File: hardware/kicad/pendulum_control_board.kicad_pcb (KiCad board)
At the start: 2 copper layers, 106.5 x 112.9 mm, 269 parts, among them IC1 STM32F411CEU6, IC2 LM358D, J1 DX07S024JJ2, Q1 BSS138, Q2 BSS138, Q3 BSS138, Q4 BSS138, Q5 2N7002, Q6 2N7002, Q7 2N7002, U1 FT231XS, U2 V_REG_317SMD, U3 V_REG_317SMD, U5 LTC6102DD, X1 5566-8, X2 5566-8, Y2 32.768kHz

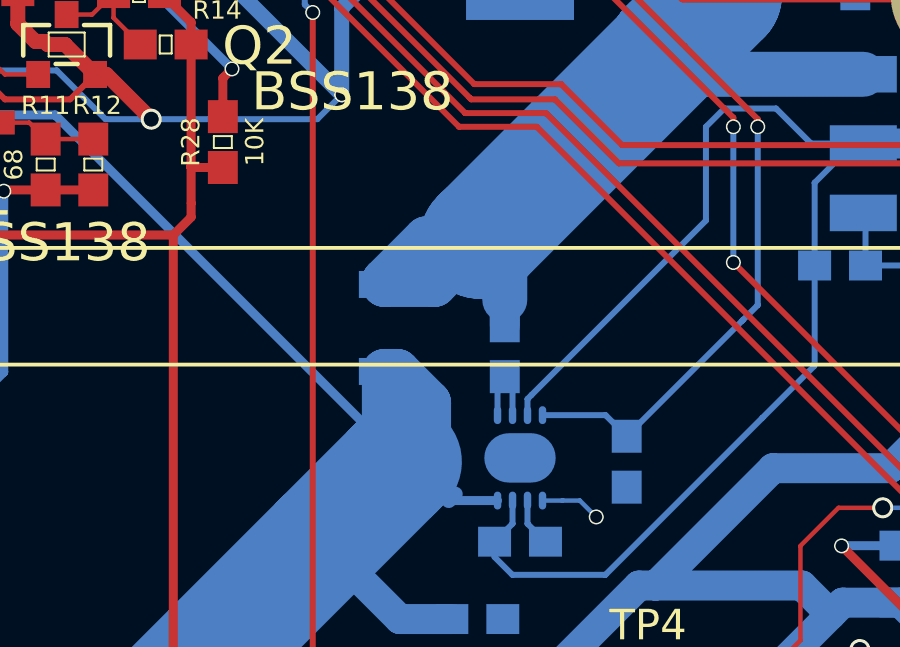
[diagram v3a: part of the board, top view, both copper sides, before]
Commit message: moved interfering resistor
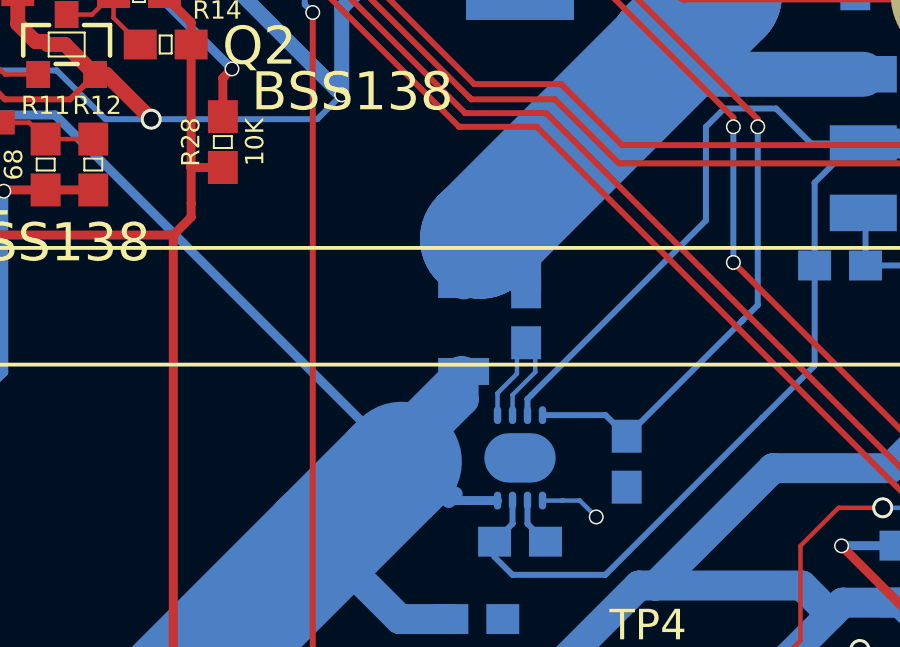
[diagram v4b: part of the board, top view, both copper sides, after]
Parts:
- moved R99 2.64 mm to (92.9, 125.0)
- moved R98 1.34 mm to (94.9, 124.7)
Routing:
- net /V_BATT: track 221.7 -> 210.1 mm
- net /N$85: track 2.77 -> 5.66 mm
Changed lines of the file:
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@@
     (links 735)
     (no_connects 0)
-    (area 47.536899 49.987999 154.177201 163.016401)
+    (area 44.840853 49.987999 154.177201 163.209581)
     (thickness 1.6)
     (drawings 6)
-    (tracks 2904)
+    (tracks 2903)
     (zones 0)
     (modules 269)
@@
   )
   (setup
-    (last_trace_width 0.3)
+    (last_trace_width 0.15)
     (user_trace_width 0.15)
     (user_trace_width 0.2)
@@
   )
   (module SPARKFUN-RESISTORS_0603 (layer B.Cu)
-    (at 94.234 125.7935 270)
+    (at 94.9452 124.6632 270)
     (descr "GENERIC 1608 (0603) PACKAGE")
     (tags "GENERIC 1608 (0603) PACKAGE")
@@
   )
   (module Resistors_SMD:R_1206 (layer B.Cu)
-    (at 90.2208 125.0188 90)
+    (at 92.8624 125.0188 90)
     (descr "Resistor SMD 1206, reflow soldering, Vishay (see dcrcw.pdf)")
     (tags "resistor 1206")
     (attr smd)
-    (fp_text reference R99 (at 0 2.3 90) (layer B.SilkS)
+    (fp_text reference R99 (at 0.254 -2.4892 90) (layer B.SilkS)
       (effects (font (size 1 1) (thickness 0.15)) (justify mirror))
     )
-    (fp_text value 1m (at 0 -2.3 90) (layer B.Fab)
+    (fp_text value 1m (at 0 -2.3 90) (layer B.Fab) hide
       (effects (font (size 1 1) (thickness 0.15)) (justify mirror))
     )
@@
   (segment (start 108.1024 148.6154) (end 106.77652 148.6154) (width 0.15) (layer B.Cu) (net 1))
   (segment (start 72.7075 101.68636) (end 72.263 101.68636) (width 0.15) (layer F.Cu) (net 1))
-  (segment (start 90.2208 123.5688) (end 90.2208 123.444) (width 1.5) (layer B.Cu) (net 2))
-  (segment (start 90.2208 123.444) (end 91.6178 122.047) (width 1.5) (layer B.Cu) (net 2))
-  (segment (start 91.6178 122.047) (end 93.4085 122.047) (width 1.5) (layer B.Cu) (net 2))
-  (segment (start 90.2208 123.5688) (end 91.8867 123.5688) (width 1.5) (layer B.Cu) (net 2))
-  (segment (start 91.8867 123.5688) (end 93.5355 121.92) (width 1.5) (layer B.Cu) (net 2))
+  (segment (start 94.9452 123.81484) (end 94.9452 120.6627) (width 1) (layer B.Cu) (net 2))
+  (segment (start 94.869 120.5865) (end 94.234 121.2215) (width 1) (layer B.Cu) (net 2))
+  (segment (start 94.9452 120.6627) (end 94.869 120.5865) (width 1) (layer B.Cu) (net 2))
+  (segment (start 92.8624 123.5688) (end 92.8624 122.5931) (width 1) (layer B.Cu) (net 2))
+  (segment (start 93.4085 122.047) (end 99.695 115.7605) (width 4) (layer B.Cu) (net 2))
+  (segment (start 93.5355 121.92) (end 93.4085 122.047) (width 4) (layer B.Cu) (net 2))
+  (segment (start 92.8624 122.5931) (end 93.5355 121.92) (width 1) (layer B.Cu) (net 2))
   (segment (start 95.08236 97.282) (end 96.5835 97.282) (width 0.2) (layer B.Cu) (net 2))
   (segment (start 96.5835 97.282) (end 98.1075 95.758) (width 0.2) (layer B.Cu) (net 2))
@@
   (segment (start 97.05086 107.4547) (end 101.1682 107.4547) (width 1.5) (layer B.Cu) (net 2))
   (segment (start 101.1682 107.4547) (end 101.473 107.7595) (width 1.5) (layer B.Cu) (net 2))
-  (segment (start 93.5355 121.92) (end 93.4085 122.047) (width 4) (layer B.Cu) (net 2))
-  (segment (start 93.4085 122.047) (end 99.695 115.7605) (width 4) (layer B.Cu) (net 2))
   (segment (start 101.473 113.919) (end 101.473 107.7595) (width 4) (layer B.Cu) (net 2))
   (segment (start 99.695 115.697) (end 101.473 113.919) (width 4) (layer B.Cu) (net 2))
   (segment (start 99.695 115.7605) (end 99.695 115.697) (width 4) (layer B.Cu) (net 2))
-  (segment (start 94.234 121.2215) (end 94.234 124.079) (width 1.5) (layer B.Cu) (net 2))
-  (segment (start 94.234 124.94514) (end 94.234 124.079) (width 1) (layer B.Cu) (net 2))
-  (segment (start 93.5355 121.92) (end 94.234 121.2215) (width 1.5) (layer B.Cu) (net 2))
-  (segment (start 94.234 121.2215) (end 92.583 122.8725) (width 1.5) (layer B.Cu) (net 2))
-  (segment (start 93.5355 121.92) (end 94.869 120.5865) (width 1) (layer B.Cu) (net 2))
-  (segment (start 94.234 121.2215) (end 94.869 120.5865) (width 1) (layer B.Cu) (net 2))
   (segment (start 104.56164 122.936) (end 104.56164 126.27356) (width 0.2) (layer B.Cu) (net 3))
   (segment (start 93.89364 132.65404) (end 94.488 133.2484) (width 0.2) (layer B.Cu) (net 3))
@@
   (segment (start 61.8236 103.9876) (end 60.94476 103.9876) (width 0.15) (layer F.Cu) (net 15))
   (segment (start 63.21298 105.37698) (end 61.8236 103.9876) (width 0.15) (layer F.Cu) (net 15))
-  (segment (start 90.2208 126.4688) (end 90.6548 126.4688) (width 1.5) (layer B.Cu) (net 16))
-  (segment (start 90.6548 126.4688) (end 91.694 127.508) (width 1.5) (layer B.Cu) (net 16))
+  (segment (start 92.8624 126.4688) (end 92.8624 127.4191) (width 1) (layer B.Cu) (net 16))
+  (segment (start 92.8624 127.4191) (end 91.694 128.5875) (width 1) (layer B.Cu) (net 16))
   (segment (start 91.694 128.5875) (end 90.805 129.4765) (width 1.5) (layer B.Cu) (net 16))
-  (segment (start 91.694 127.508) (end 91.694 128.5875) (width 1.5) (layer B.Cu) (net 16))
-  (segment (start 90.2208 126.4688) (end 90.2208 128.8923) (width 1.5) (layer B.Cu) (net 16))
+  (segment (start 92.8624 126.4688) (end 92.7332 126.4688) (width 1) (layer B.Cu) (net 16))
+  (segment (start 92.7332 126.4688) (end 90.805 128.397) (width 1) (layer B.Cu) (net 16))
+  (segment (start 90.805 128.397) (end 90.805 129.4765) (width 1.5) (layer B.Cu) (net 16))
   (segment (start 90.2208 128.8923) (end 90.805 129.4765) (width 1.5) (layer B.Cu) (net 16))
   (segment (start 92.47124 134.7216) (end 90.7288 134.7216) (width 1) (layer B.Cu) (net 16))
@@
   (via (at 56.896 113.792) (size 0.5) (drill 0.4) (layers F.Cu B.Cu) (net 16))
   (segment (start 92.583 130.556) (end 92.3671 130.7719) (width 0.5) (layer B.Cu) (net 16))
-  (segment (start 90.805 128.397) (end 90.805 129.4765) (width 1.5) (layer B.Cu) (net 16))
   (segment (start 90.551 128.651) (end 90.551 129.7305) (width 1) (layer B.Cu) (net 16))
   (segment (start 93.9927 130.7719) (end 92.3671 130.7719) (width 0.3) (layer B.Cu) (net 16))
@@
   (segment (start 59.69 72.898) (end 59.69 66.02476) (width 0.2) (layer F.Cu) (net 170))
   (segment (start 59.69 66.02476) (end 61.31052 64.40424) (width 0.2) (layer F.Cu) (net 170))
-  (segment (start 94.49308 127.92456) (end 94.49308 126.90094) (width 0.2) (layer B.Cu) (net 171))
-  (segment (start 94.49308 126.90094) (end 94.234 126.64186) (width 0.2) (layer B.Cu) (net 171))
-  (segment (start 93.9927 127.92456) (end 93.9927 126.88316) (width 0.2) (layer B.Cu) (net 171))
-  (segment (start 93.9927 126.88316) (end 94.234 126.64186) (width 0.2) (layer B.Cu) (net 171))
+  (segment (start 94.49308 127.92456) (end 94.49308 127.24892) (width 0.15) (layer B.Cu) (net 171) (status 400000))
+  (segment (start 95.25 126.492) (end 95.25 125.81636) (width 0.15) (layer B.Cu) (net 171) (status 800000))
+  (segment (start 94.49308 127.24892) (end 95.25 126.492) (width 0.15) (layer B.Cu) (net 171))
+  (segment (start 95.25 125.81636) (end 94.9452 125.51156) (width 0.15) (layer B.Cu) (net 171) (status C00000))
+  (segment (start 94.9452 125.51156) (end 94.9452 125.6792) (width 0.15) (layer B.Cu) (net 171) (status C00000))
+  (segment (start 94.9452 125.6792) (end 94.6404 125.984) (width 0.15) (layer B.Cu) (net 171) (status C00000))
+  (segment (start 94.6404 125.984) (end 94.6404 126.5428) (width 0.15) (layer B.Cu) (net 171) (status 400000))
+  (segment (start 94.6404 126.5428) (end 93.9927 127.1905) (width 0.15) (layer B.Cu) (net 171))
+  (segment (start 93.9927 127.1905) (end 93.9927 127.92456) (width 0.15) (layer B.Cu) (net 171) (status 800000))
   (segment (start 67.5767 102.87508) (end 67.5767 101.61016) (width 0.15) (layer F.Cu) (net 172))
   (segment (start 67.5767 101.61016) (end 67.945 101.24186) (width 0.15) (layer F.Cu) (net 172))
